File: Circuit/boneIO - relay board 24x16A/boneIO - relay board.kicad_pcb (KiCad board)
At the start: 2 copper layers, 197 x 102 mm, 68 parts, among them J1 Screw_Terminal_01x04, J10 Screw_Terminal_01x04, J11 Screw_Terminal_01x04, J12 Screw_Terminal_01x04, J13 Screw_Terminal_01x04, J14 Conn_02x04_Odd_Even, J2 Screw_Terminal_01x04, J4 Screw_Terminal_01x04, J5 Screw_Terminal_01x04, J6 Screw_Terminal_01x04, J7 Screw_Terminal_01x04, J8 Screw_Terminal_01x04, J9 Screw_Terminal_01x04, K1 RM85-2011-35-1005, K10 RM85-2011-35-1005, K11 RM85-2011-35-1005, K12 RM85-2011-35-1005, K13 RM85-2011-35-1005, K14 RM85-2011-35-1005, K15 RM85-2011-35-1005, K16 RM85-2011-35-1005, K17 RM85-2011-35-1005, K18 RM85-2011-35-1005, K19 RM85-2011-35-1005, K2 RM85-2011-35-1005, K20 RM85-2011-35-1005, K21 RM85-2011-35-1005, K22 RM85-2011-35-1005, K23 RM85-2011-35-1005, K24 RM85-2011-35-1005, K3 RM85-2011-35-1005, K4 RM85-2011-35-1005, K5 RM85-2011-35-1005, K6 RM85-2011-35-1005, K7 RM85-2011-35-1005, K8 RM85-2011-35-1005, K9 RM85-2011-35-1005, SW1 SW_DIP_x03, SW2 SW_DIP_x03, SW3 SW_DIP_x03, U1 MCP9808_MSOP, U2 MCP23017_SS, U3 MCP23017_SS, U4 ULN2803A, U5 ULN2803A, U6 ULN2803A

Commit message: DRC Cleanup and some other small fixes
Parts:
- removed J14: Conn_02x04_Odd_Even, Connector_PinHeader_2.54mm:PinHeader_2x04_P2.54mm_Vertical
- added J3: Conn_02x04_Odd_Even, ph80ds-21:PinHeader_2x04_P2.54mm_Vertical, F.Cu at (378.1, 315.7)
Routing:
- net (no net): track 0.00 -> 18.2 mm
- net Net-(J10-Pad1): track 48.5 -> 52.0 mm
- net Net-(J8-Pad3): track 48.5 -> 52.0 mm
- net Net-(J12-Pad3): track 48.5 -> 52.0 mm
- net Net-(J10-Pad3): track 48.5 -> 52.0 mm
- net Net-(J9-Pad3): track 48.5 -> 52.0 mm
- net Net-(J11-Pad1): track 48.5 -> 52.0 mm
- net Net-(J11-Pad3): track 48.5 -> 52.0 mm
- net Net-(J8-Pad1): track 48.5 -> 52.0 mm
- net Net-(J9-Pad1): track 48.5 -> 52.0 mm
- net Net-(J7-Pad1): track 48.5 -> 52.0 mm
- net Net-(J7-Pad3): track 48.5 -> 52.0 mm
- net Net-(J12-Pad1): track 48.5 -> 52.0 mm
- net Net-(J13-Pad3): track 48.5 -> 51.4 mm
- net Net-(J5-Pad3): track 48.5 -> 51.4 mm
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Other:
- board text removed: "relay board 24x16A v0.2"

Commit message: Some more small fixes
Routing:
- net (no net): track 18.2 -> 0.00 mm
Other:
- board text added: "Relay Board 24x16A"

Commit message: final PCB version
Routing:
- net VCC: track 537.3 -> 545.6 mm, vias 0 -> 6

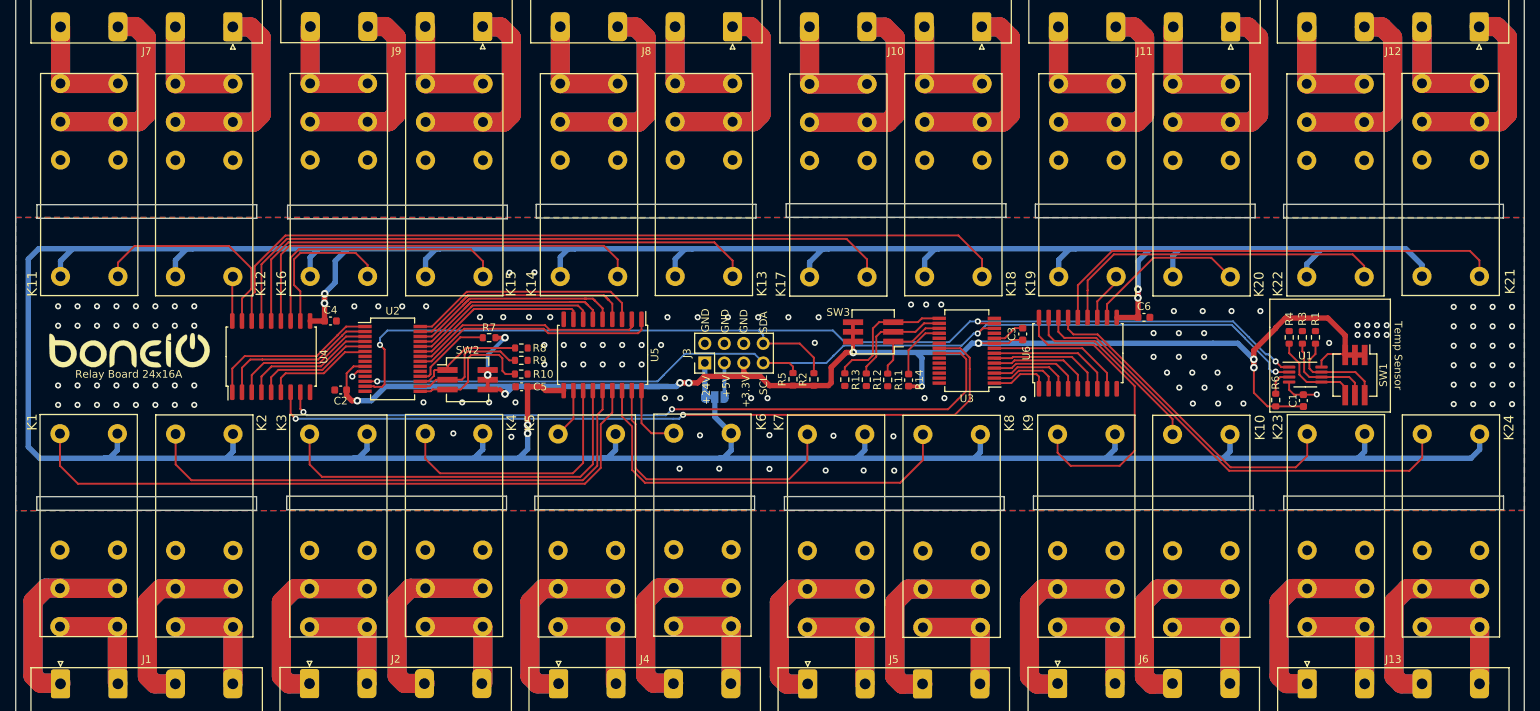
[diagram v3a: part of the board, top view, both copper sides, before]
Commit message: cleanup relay board 24x16
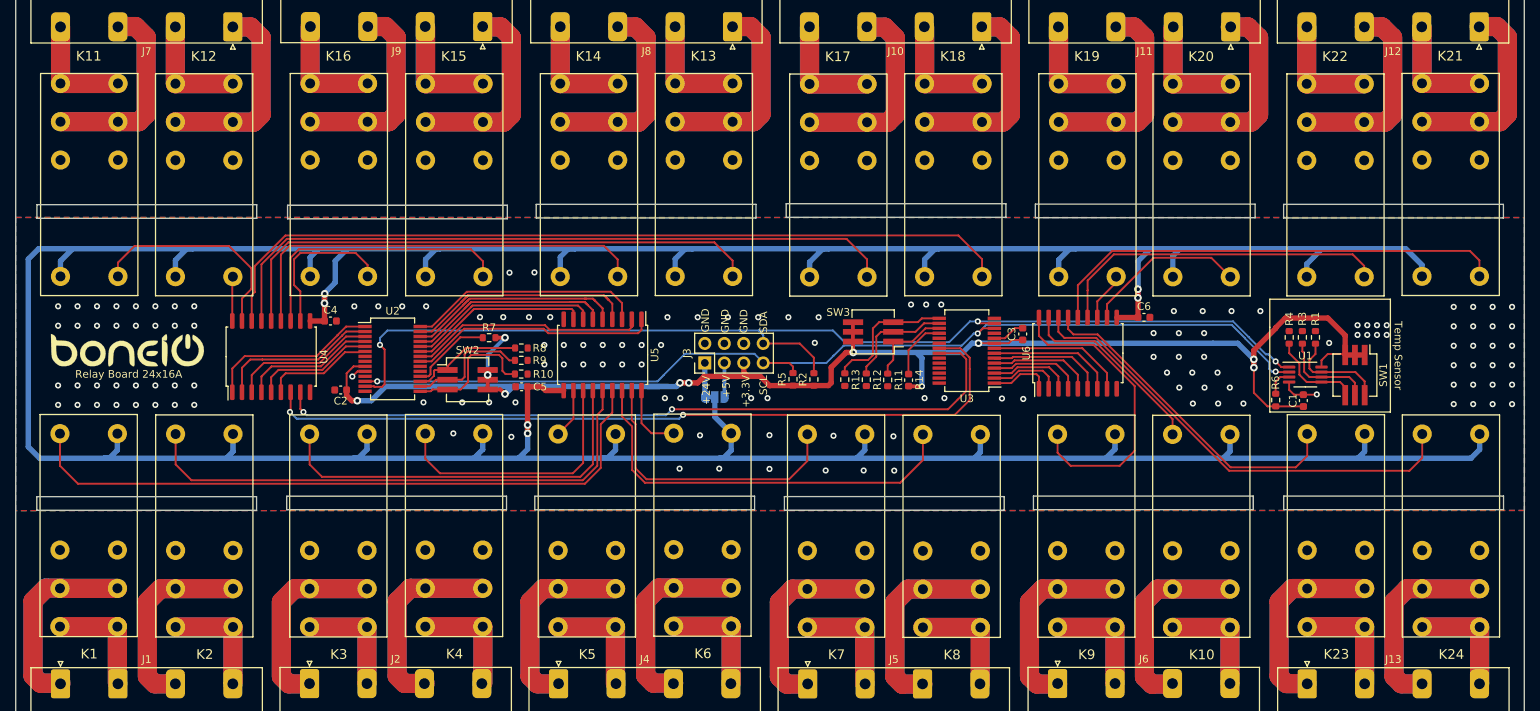
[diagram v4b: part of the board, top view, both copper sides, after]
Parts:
- removed the G*** at (303.0, 314.1)
- added G***: LOGO, boneIO:boneIO_LOGO, F.Cu at (302.7, 314.0)
- J3: footprint ph80ds-21:PinHeader_2x04_P2.54mm_Vertical -> boneIO:PinHeader_2x04_P2.54mm_Vertical
- K1, K10, K11, K12, K13, K14, K15, K16, K17, K18, K19, K2, K20, K21, K22, K23, K24, K3, K4, K5, K6, K7, K8, K9: footprint boneIO - RM85:RM852011351005_1 -> boneIO:RM852011351005_1

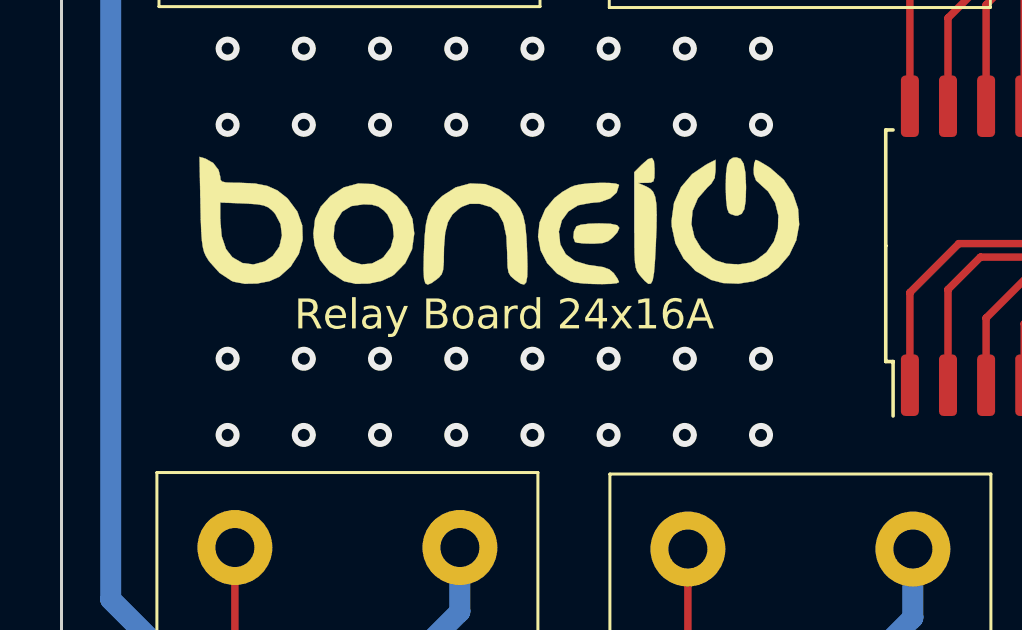
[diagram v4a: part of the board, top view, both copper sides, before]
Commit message: Changed board labels
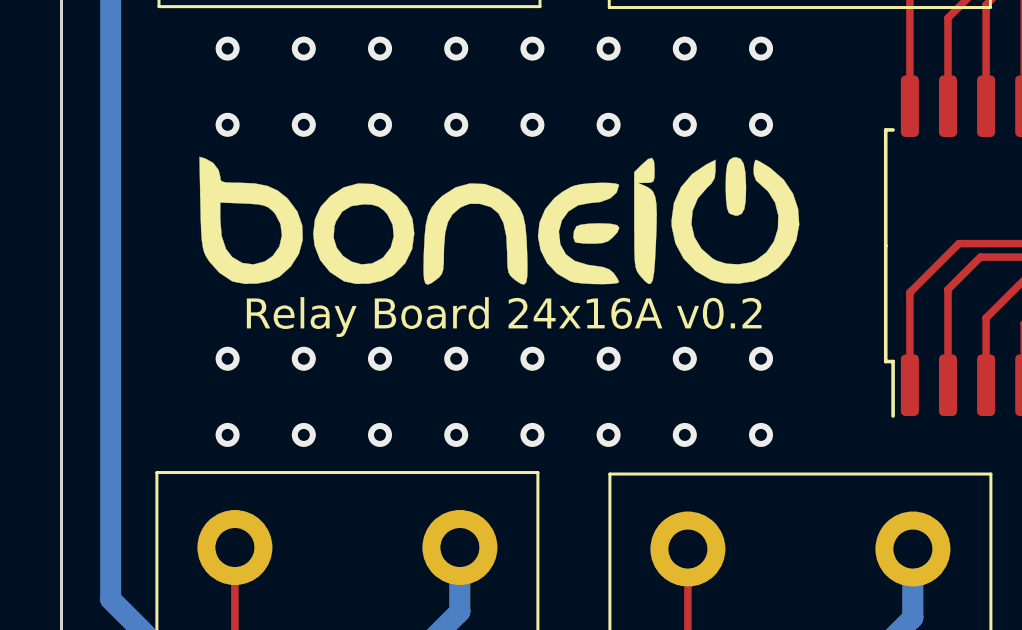
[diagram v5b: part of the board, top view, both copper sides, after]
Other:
- board text added: "Relay Board 24x16A v0.2"
- board text removed: "Relay Board 24x16A"

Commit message: 24x16 cleanup
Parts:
- removed the G*** at (302.7, 314.0)
- removed K1, K10, K11, K12, K13, K14, K15, K16, K17, K18, K19, K2, K20, K21, K22, K23, K24, K3, K4, K5, K6, K7, K8, K9: RM85-2011-35-1005, boneIO:RM852011351005_1
- added G***: LOGO, Symbol:boneIO_LOGO_srednie, F.Cu at (303.0, 314.1)
- added U10: RM85-2011-35-1024, boneIO - relay board 24x16A:RM852011351024, F.Cu at (341.6, 345.1)
- added U11: RM85-2011-35-1024, boneIO - relay board 24x16A:RM852011351024, F.Cu at (359.0, 345.2)
- added U12: RM85-2011-35-1024, boneIO - relay board 24x16A:RM852011351024, F.Cu at (374.1, 345.1)
- added U13: RM85-2011-35-1024, boneIO - relay board 24x16A:RM852011351024, F.Cu at (391.5, 345.2)
- added U14: RM85-2011-35-1024, boneIO - relay board 24x16A:RM852011351024, F.Cu at (406.6, 345.2)
- added U15: RM85-2011-35-1024, boneIO - relay board 24x16A:RM852011351024, F.Cu at (424.2, 345.2)
- added U16: RM85-2011-35-1024, boneIO - relay board 24x16A:RM852011351024, F.Cu at (439.2, 345.2)
- added U17: RM85-2011-35-1024, boneIO - relay board 24x16A:RM852011351024, F.Cu at (301.5, 284.2)
- added U18: RM85-2011-35-1024, boneIO - relay board 24x16A:RM852011351024, F.Cu at (316.5, 284.2)
- added U19: RM85-2011-35-1024, boneIO - relay board 24x16A:RM852011351024, F.Cu at (381.8, 284.2)
- added U20: RM85-2011-35-1024, boneIO - relay board 24x16A:RM852011351024, F.Cu at (366.8, 284.2)
- added U21: RM85-2011-35-1024, boneIO - relay board 24x16A:RM852011351024, F.Cu at (349.2, 284.2)
- added U22: RM85-2011-35-1024, boneIO - relay board 24x16A:RM852011351024, F.Cu at (334.1, 284.2)
- added U23: RM85-2011-35-1024, boneIO - relay board 24x16A:RM852011351024, F.Cu at (399.3, 284.3)
- added U24: RM85-2011-35-1024, boneIO - relay board 24x16A:RM852011351024, F.Cu at (414.3, 284.2)
- added U25: RM85-2011-35-1024, boneIO - relay board 24x16A:RM852011351024, F.Cu at (431.8, 284.2)
- added U26: RM85-2011-35-1024, boneIO - relay board 24x16A:RM852011351024, F.Cu at (446.8, 284.2)
- added U27: RM85-2011-35-1024, boneIO - relay board 24x16A:RM852011351024, F.Cu at (479.3, 284.2)
- added U28: RM85-2011-35-1024, boneIO - relay board 24x16A:RM852011351024, F.Cu at (464.2, 284.3)
- added U29: RM85-2011-35-1024, boneIO - relay board 24x16A:RM852011351024, F.Cu at (456.8, 345.2)
- added U30: RM85-2011-35-1024, boneIO - relay board 24x16A:RM852011351024, F.Cu at (471.8, 345.2)
- added U7: RM85-2011-35-1024, boneIO - relay board 24x16A:RM852011351024, F.Cu at (293.9, 345.1)
- added U8: RM85-2011-35-1024, boneIO - relay board 24x16A:RM852011351024, F.Cu at (309.0, 345.2)
- added U9: RM85-2011-35-1024, boneIO - relay board 24x16A:RM852011351024, F.Cu at (326.5, 345.2)
- J3: footprint boneIO:PinHeader_2x04_P2.54mm_Vertical -> boneIO - relay board 24x16A:PinHeader_2x04_P2.54mm_Vertical
- U1: value MCP9808_MSOP -> MCP9808-E_MS; footprint Package_SO:MSOP-8_3x3mm_P0.65mm -> boneIO - relay board 24x16A:SOP65P490X110-8N
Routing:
- net VCC: track 545.6 -> 547.0 mm
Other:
- board text added: "Relay Board 24x16A"
- board text removed: "Relay Board 24x16A v0.2"
